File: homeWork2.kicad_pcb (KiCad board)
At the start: 2 copper layers, 125 x 99.9 mm, 43 parts, among them J1 Barrel_Jack_Switch_SMT, U1 LM7805_TO220

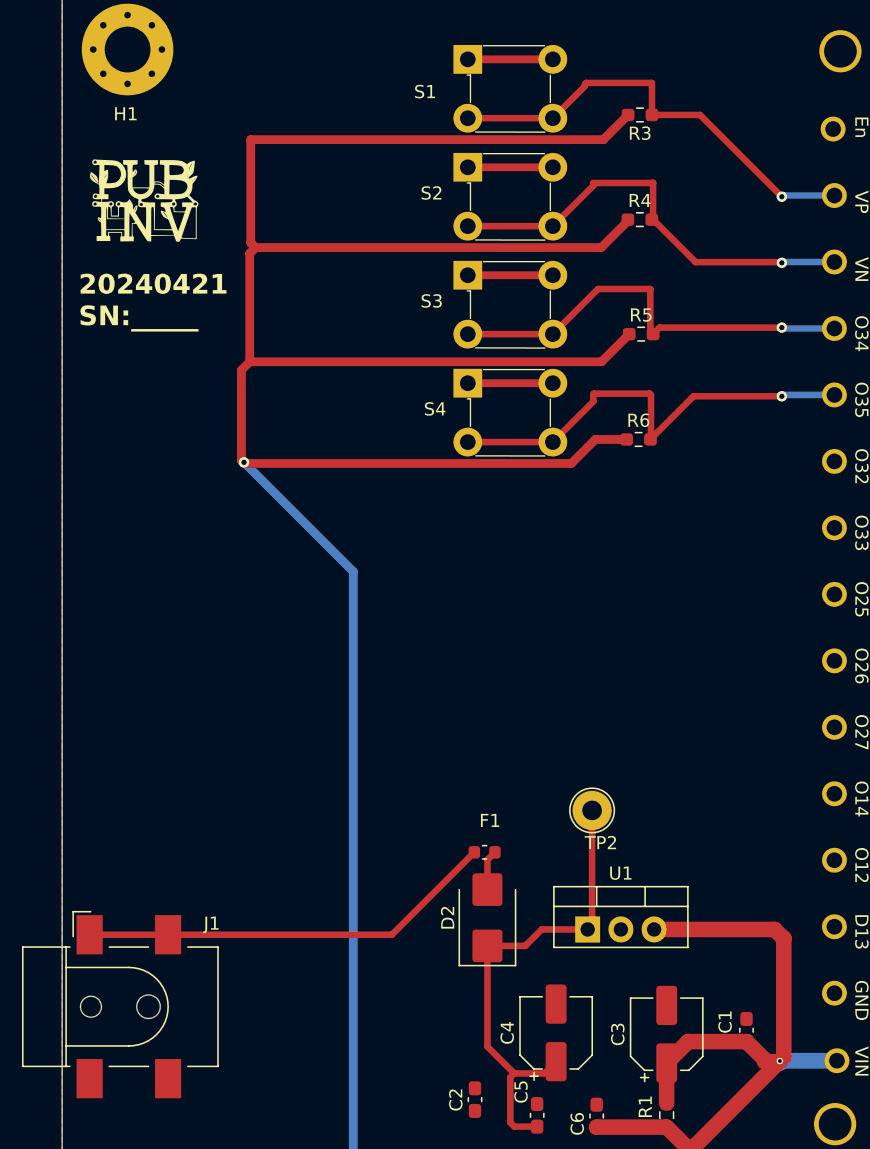
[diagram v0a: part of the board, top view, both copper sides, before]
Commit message: Added text box capturing the calculations for setting the currect in LED.
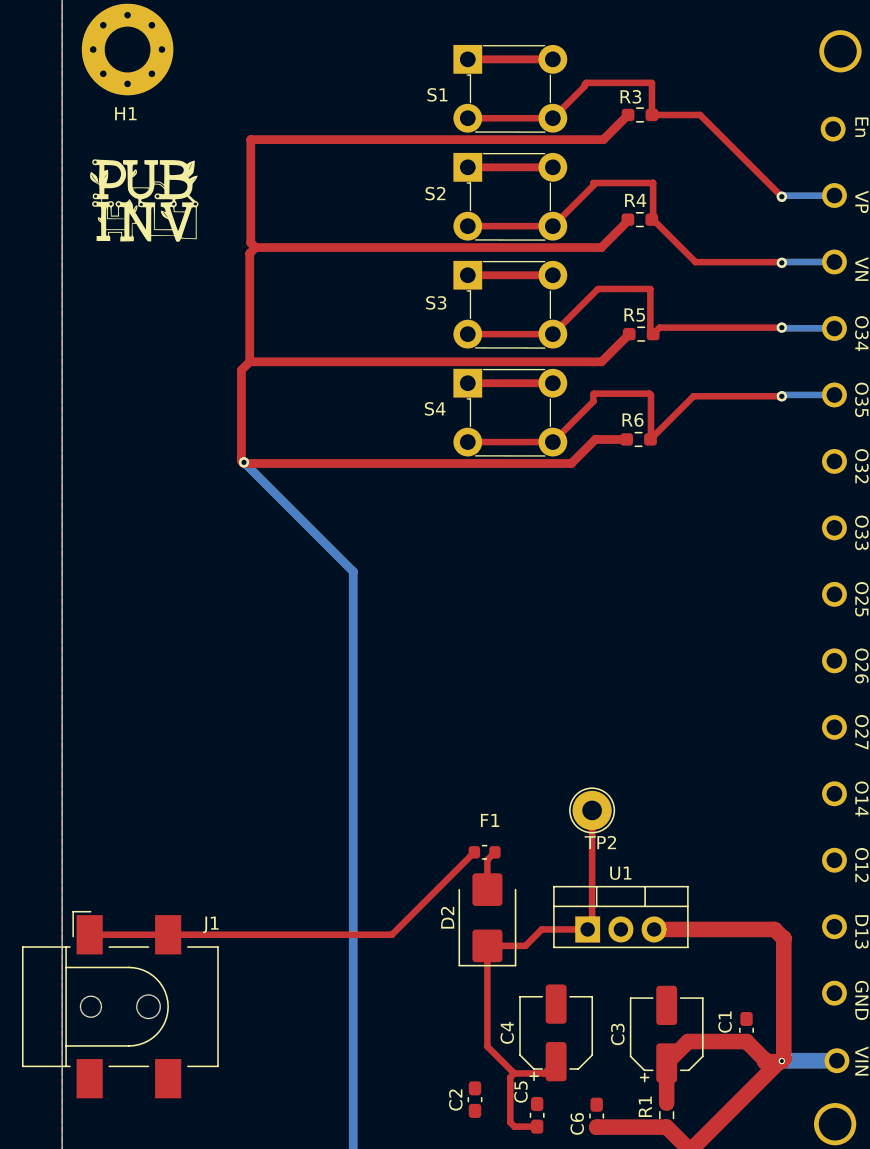
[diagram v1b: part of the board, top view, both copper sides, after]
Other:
- board text removed: "20240421 SN:_____"
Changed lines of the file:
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@@
     (property "ki_keywords" "450-1804-ND FSMJ")
     (attr through_hole)
-    (fp_text reference "S2" (at -2.75 2 180) (layer "F.SilkS")
+    (fp_text reference "S2" (at -2.45 2.05 180) (layer "F.SilkS")
         (effects (font (size 1 1) (thickness 0.15)))
     )
@@
     (property "ki_keywords" "R res resistor")
     (attr smd)
-    (fp_text reference "R4" (at 0 -1.43) (layer "F.SilkS")
+    (fp_text reference "R4" (at -0.35 -1.43) (layer "F.SilkS")
         (effects (font (size 1 1) (thickness 0.15)))
     )
@@
     (property "ki_keywords" "R res resistor")
     (attr smd)
-    (fp_text reference "R3" (at 0 -1.43) (layer "F.SilkS")
+    (fp_text reference "R3" (at 0.7125 1.35) (layer "F.SilkS")
         (effects (font (size 1 1) (thickness 0.15)))
     )
-    (fp_text value "10 k" (at 0 1.43) (layer "F.Fab")
+    (fp_text value "10 k" (at -1.4875 -1.5) (layer "F.Fab")
         (effects (font (size 1 1) (thickness 0.15)))
     )
@@
     (property "ki_keywords" "450-1804-ND FSMJ")
     (attr through_hole)
-    (fp_text reference "S1" (at -3.25 2.5 180) (layer "F.SilkS")
+    (fp_text reference "S1" (at -2.3 2.75 180) (layer "F.SilkS")
         (effects (font (size 1 1) (thickness 0.15)))
     )
@@
     (property "ki_keywords" "R res resistor")
     (attr smd)
-    (fp_text reference "R5" (at 0 -1.43) (layer "F.SilkS")
+    (fp_text reference "R5" (at -0.5 -1.43) (layer "F.SilkS")
         (effects (font (size 1 1) (thickness 0.15)))
     )
@@
     (property "ki_keywords" "450-1804-ND FSMJ")
     (attr through_hole)
-    (fp_text reference "S3" (at -2.75 2 180) (layer "F.SilkS")
+    (fp_text reference "S3" (at -2.4 2.15 180) (layer "F.SilkS")
         (effects (font (size 1 1) (thickness 0.15)))
     )
@@
     (property "ki_keywords" "R res resistor")
     (attr smd)
-    (fp_text reference "R6" (at 0 -1.43) (layer "F.SilkS")
+    (fp_text reference "R6" (at -0.45 -1.45) (layer "F.SilkS")
         (effects (font (size 1 1) (thickness 0.15)))
     )
@@
   (gr_rect (start 50 50) (end 175 149.95)
     (stroke (width 0.1) (type default)) (fill none) (layer "Edge.Cuts"))
-  (gr_text "20240421\nSN:_____" (at 51.25 76.25) (layer "F.SilkS")
-    (effects (font (size 1.5 1.5) (thickness 0.3) bold) (justify left bottom))
-  )
+  (gr_text_box "20240421\nSN:_____"
+    (start 52 72.3) (end 61 79.3) (layer "F.SilkS")
+      (effects (font (size 1 1) (thickness 0.15)) (justify left top))
+    (stroke (width 0.2) (type solid))  )
   (dimension (type aligned) (layer "Dwgs.User")
     (pts (xy 50 150) (xy 170 150))
@@
   (segment (start 86.3 137.3125) (end 84.5625 137.3125) (width 0.5) (layer "F.Cu") (net 2))
   (segment (start 102.3 130.8125) (end 97.8375 130.8125) (width 1.19) (layer "F.Cu") (net 3))
-  (segment (start 104.8 132.35) (end 104.85 132.3) (width 1.19) (layer "F.Cu") (net 3))
   (segment (start 97.75 140.15) (end 97.75 138.9) (width 1.19) (layer "F.Cu") (net 3))
-  (segment (start 105.15 122.95) (end 105.15 132) (width 1.19) (layer "F.Cu") (net 3))
   (segment (start 103.7 132.2125) (end 103.7 132.35) (width 1.19) (layer "F.Cu") (net 3))
+  (segment (start 97.75 139.4) (end 97.75 140.15) (width 1.19) (layer "F.Cu") (net 3))
   (segment (start 91 143.25) (end 92.9125 143.25) (width 1.19) (layer "F.Cu") (net 3))
   (segment (start 96.2 137.35) (end 90.8625 137.35) (width 1.19) (layer "F.Cu") (net 3))
@@
   (segment (start 90.8625 137.35) (end 90.85 137.3625) (width 1.19) (layer "F.Cu") (net 3))
   (segment (start 103.7 132.35) (end 103.8375 132.35) (width 1.19) (layer "F.Cu") (net 3))
-  (segment (start 105.15 132) (end 104.85 132.3) (width 1.19) (layer "F.Cu") (net 3))
   (segment (start 104.445 122.245) (end 105.1 122.9) (width 1.19) (layer "F.Cu") (net 3))
+  (segment (start 105 132.3) (end 104.95 132.35) (width 1.19) (layer "F.Cu") (net 3))
+  (segment (start 104.85 132.3) (end 97.75 139.4) (width 1.19) (layer "F.Cu") (net 3))
   (segment (start 97.8375 130.8125) (end 96.2 132.45) (width 1.19) (layer "F.Cu") (net 3))
+  (segment (start 104.95 132.35) (end 103.7 132.35) (width 1.19) (layer "F.Cu") (net 3))
+  (segment (start 105 132.3) (end 105.15 132.15) (width 1.19) (layer "F.Cu") (net 3))
   (segment (start 97.75 141.75) (end 97.75 140.15) (width 1.19) (layer "F.Cu") (net 3))
   (segment (start 96.2 132.45) (end 96.2 135.525) (width 1.19) (layer "F.Cu") (net 3))
   (segment (start 99.15 143.15) (end 101.85 143.15) (width 1.19) (layer "F.Cu") (net 3))
-  (segment (start 104.85 132.3) (end 97.75 139.4) (width 1.19) (layer "F.Cu") (net 3))
-  (segment (start 97.75 139.4) (end 97.75 140.15) (width 1.19) (layer "F.Cu") (net 3))
-  (segment (start 103.7 132.35) (end 104.8 132.35) (width 1.19) (layer "F.Cu") (net 3))
-  (via (at 104.85 132.3) (size 0.5) (drill 0.3) (layers "F.Cu" "B.Cu") (net 3))
-  (segment (start 104.85 132.3) (end 104.85 132.45) (width 1.19) (layer "B.Cu") (net 3))
-  (segment (start 104.85 132.45) (end 105 132.3) (width 1.19) (layer "B.Cu") (net 3))
+  (segment (start 105 132.3) (end 104.85 132.3) (width 1.19) (layer "F.Cu") (net 3))
+  (segment (start 105.15 132.15) (end 105.15 122.95) (width 1.19) (layer "F.Cu") (net 3))
+  (via (at 105 132.3) (size 0.5) (drill 0.3) (layers "F.Cu" "B.Cu") (net 3))
   (segment (start 105.023 132.277) (end 105 132.3) (width 1.19) (layer "B.Cu") (net 3))
-  (segment (start 105 132.3) (end 104.85 132.3) (width 1.19) (layer "B.Cu") (net 3))
   (segment (start 109.2107 132.277) (end 105.023 132.277) (width 1.19) (layer "B.Cu") (net 3))
   (segment (start 82.5 119.2) (end 82.5 116.925) (width 0.5) (layer "F.Cu") (net 5))

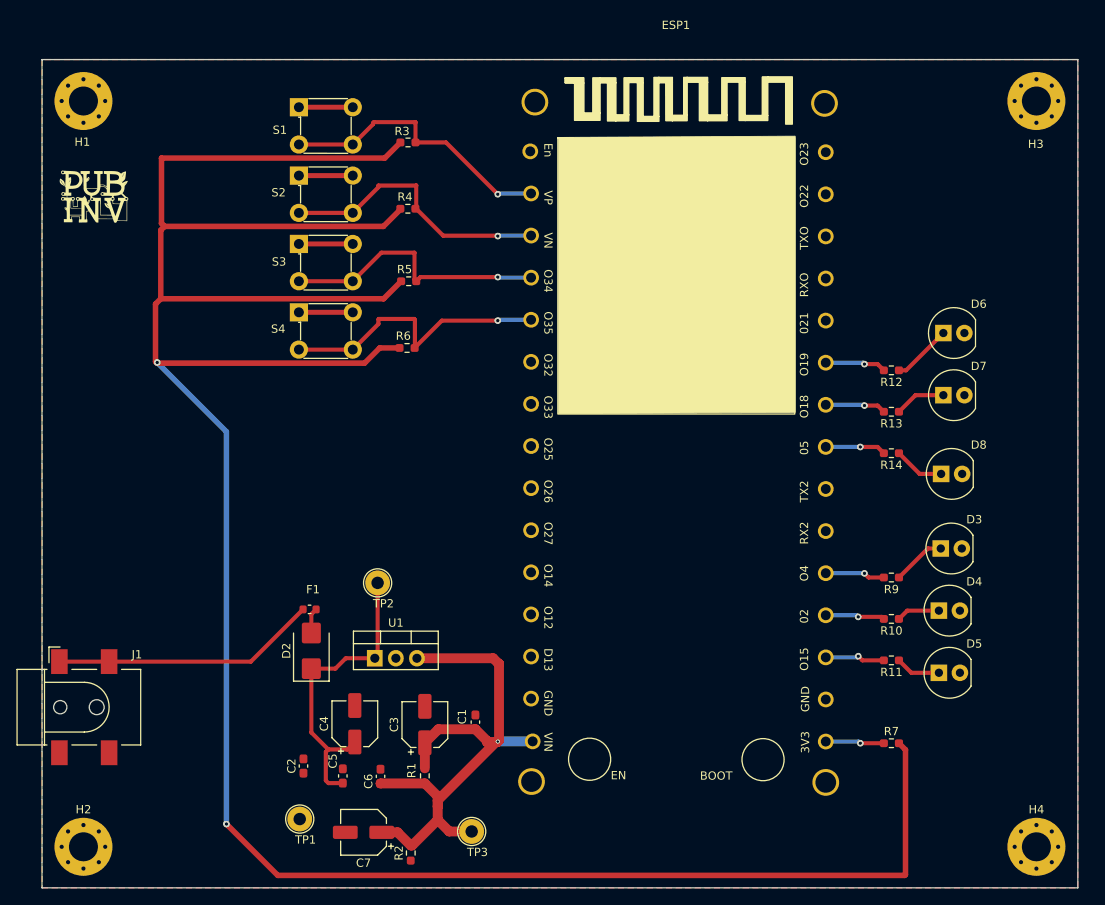
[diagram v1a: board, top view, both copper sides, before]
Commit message: Functions have been added to the switches and LEDs, and silkscreen has been included on the PCB to indicate these functions.
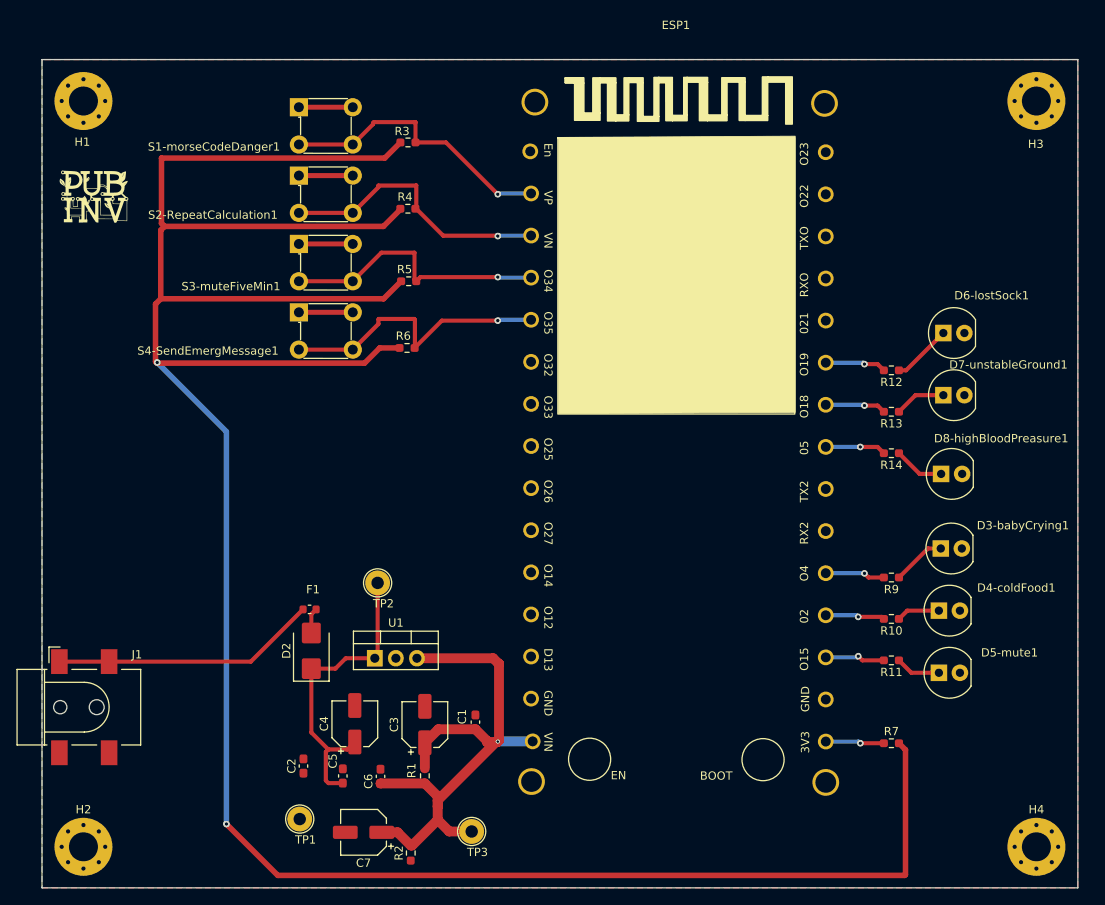
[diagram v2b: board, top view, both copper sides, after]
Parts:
- renumbered D3 to D3-babyCrying1, D4 to D4-coldFood1, D5 to D5-mute1, D6 to D6-lostSock1, D7 to D7-unstableGround1, D8 to D8-highBloodPreasure1, S1 to S1-morseCodeDanger1, S2 to S2-RepeatCalculation1, S3 to S3-muteFiveMin1, S4 to S4-SendEmergMessage1
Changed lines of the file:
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@@
   (net 4 "Net-(D1-Pad1)")
   (net 5 "Net-(D2-A)")
-  (net 6 "Net-(D3-Pad1)")
-  (net 7 "Net-(D4-Pad1)")
-  (net 8 "Net-(D5-Pad1)")
-  (net 9 "Net-(D6-Pad1)")
-  (net 10 "Net-(D7-Pad1)")
-  (net 11 "Net-(D8-Pad1)")
+  (net 6 "Net-(D3-babyCrying1-Pad1)")
+  (net 7 "Net-(D4-coldFood1-Pad1)")
+  (net 8 "Net-(D5-mute1-Pad1)")
+  (net 9 "Net-(D6-lostSock1-Pad1)")
+  (net 10 "Net-(D7-unstableGround1-Pad1)")
+  (net 11 "Net-(D8-highBloodPreasure1-Pad1)")
   (net 12 "unconnected-(ESP1-O13-Pad3)")
   (net 13 "Net-(F1-Pad2)")
@@
       (stroke (width 0.1) (type solid)) (layer "F.Fab"))
     (pad "1" smd roundrect (at -0.9125 0 180) (size 0.975 0.95) (layers "F.Cu" "F.Paste" "F.Mask") (roundrect_rratio 0.25)
-      (net 11 "Net-(D8-Pad1)") (pintype "passive"))
+      (net 11 "Net-(D8-highBloodPreasure1-Pad1)") (pintype "passive"))
     (pad "2" smd roundrect (at 0.9125 0 180) (size 0.975 0.95) (layers "F.Cu" "F.Paste" "F.Mask") (roundrect_rratio 0.25)
       (net 19 "Net-(ESP1-O5)") (pintype "passive"))
@@
     (property "ki_keywords" "160-1772-ND")
     (attr through_hole)
-    (fp_text reference "D6" (at 1.73 -3.5) (layer "F.SilkS")
+    (fp_text reference "D6-lostSock1" (at 3.29 -4.525) (layer "F.SilkS")
         (effects (font (size 1 1) (thickness 0.15)))
     )
@@
       (stroke (width 0.1) (type solid)) (layer "F.Fab"))
     (pad "1" thru_hole rect (at -2.54 0) (size 2 2) (drill 1) (layers "*.Cu" "*.Mask")
-      (net 9 "Net-(D6-Pad1)") (pintype "passive"))
+      (net 9 "Net-(D6-lostSock1-Pad1)") (pintype "passive"))
     (pad "2" thru_hole circle (at 0 0) (size 2 2) (drill 1) (layers "*.Cu" "*.Mask")
       (net 1 "GND") (pintype "passive"))
@@
     (property "ki_keywords" "450-1804-ND FSMJ")
     (attr through_hole)
-    (fp_text reference "S2" (at -2.45 2.05 180) (layer "F.SilkS")
+    (fp_text reference "S2-RepeatCalculation1" (at -10.375 4.75 180) (layer "F.SilkS")
         (effects (font (size 1 1) (thickness 0.15)))
     )
@@
       (stroke (width 0.1) (type solid)) (layer "F.Fab"))
     (pad "1" smd roundrect (at -0.9125 0 180) (size 0.975 0.95) (layers "F.Cu" "F.Paste" "F.Mask") (roundrect_rratio 0.25)
-      (net 9 "Net-(D6-Pad1)") (pintype "passive"))
+      (net 9 "Net-(D6-lostSock1-Pad1)") (pintype "passive"))
     (pad "2" smd roundrect (at 0.9125 0 180) (size 0.975 0.95) (layers "F.Cu" "F.Paste" "F.Mask") (roundrect_rratio 0.25)
       (net 17 "Net-(ESP1-O19)") (pintype "passive"))
@@
       (stroke (width 0.1) (type solid)) (layer "F.Fab"))
     (pad "1" smd roundrect (at -0.9125 0 180) (size 0.975 0.95) (layers "F.Cu" "F.Paste" "F.Mask") (roundrect_rratio 0.25)
-      (net 6 "Net-(D3-Pad1)") (pintype "passive"))
+      (net 6 "Net-(D3-babyCrying1-Pad1)") (pintype "passive"))
     (pad "2" smd roundrect (at 0.9125 0 180) (size 0.975 0.95) (layers "F.Cu" "F.Paste" "F.Mask") (roundrect_rratio 0.25)
       (net 14 "Net-(ESP1-O4)") (pintype "passive"))
@@
       (stroke (width 0.1) (type solid)) (layer "F.Fab"))
     (pad "1" smd roundrect (at -0.9125 0 180) (size 0.975 0.95) (layers "F.Cu" "F.Paste" "F.Mask") (roundrect_rratio 0.25)
-      (net 7 "Net-(D4-Pad1)") (pintype "passive"))
+      (net 7 "Net-(D4-coldFood1-Pad1)") (pintype "passive"))
     (pad "2" smd roundrect (at 0.9125 0 180) (size 0.975 0.95) (layers "F.Cu" "F.Paste" "F.Mask") (roundrect_rratio 0.25)
       (net 15 "Net-(ESP1-O2)") (pintype "passive"))
@@
     (property "ki_keywords" "160-1772-ND")
     (attr through_hole)
-    (fp_text reference "D3" (at 1.5 -3.5) (layer "F.SilkS")
+    (fp_text reference "D3-babyCrying1" (at 7.375 -2.775) (layer "F.SilkS")
         (effects (font (size 1 1) (thickness 0.15)))
     )
@@
       (stroke (width 0.1) (type solid)) (layer "F.Fab"))
     (pad "1" thru_hole rect (at -2.54 0) (size 2 2) (drill 1) (layers "*.Cu" "*.Mask")
-      (net 6 "Net-(D3-Pad1)") (pintype "passive"))
+      (net 6 "Net-(D3-babyCrying1-Pad1)") (pintype "passive"))
     (pad "2" thru_hole circle (at 0 0) (size 2 2) (drill 1) (layers "*.Cu" "*.Mask")
       (net 1 "GND") (pintype "passive"))
@@
     (property "ki_keywords" "450-1804-ND FSMJ")
     (attr through_hole)
-    (fp_text reference "S1" (at -2.3 2.75 180) (layer "F.SilkS")
+    (fp_text reference "S1-morseCodeDanger1" (at -10.25 4.775 180) (layer "F.SilkS")
         (effects (font (size 1 1) (thickness 0.15)))
     )
@@
     (property "ki_keywords" "160-1772-ND")
     (attr through_hole)
-    (fp_text reference "D5" (at 1.73 -3.5) (layer "F.SilkS")
+    (fp_text reference "D5-mute1" (at 5.98 -2.425) (layer "F.SilkS")
         (effects (font (size 1 1) (thickness 0.15)))
     )
@@
       (stroke (width 0.1) (type solid)) (layer "F.Fab"))
     (pad "1" thru_hole rect (at -2.54 0) (size 2 2) (drill 1) (layers "*.Cu" "*.Mask")
-      (net 8 "Net-(D5-Pad1)") (pintype "passive"))
+      (net 8 "Net-(D5-mute1-Pad1)") (pintype "passive"))
     (pad "2" thru_hole circle (at 0 0) (size 2 2) (drill 1) (layers "*.Cu" "*.Mask")
       (net 1 "GND") (pintype "passive"))
@@
     (property "ki_keywords" "450-1804-ND FSMJ")
     (attr through_hole)
-    (fp_text reference "S3" (at -2.4 2.15 180) (layer "F.SilkS")
+    (fp_text reference "S3-muteFiveMin1" (at -8.2 5.125 180) (layer "F.SilkS")
         (effects (font (size 1 1) (thickness 0.15)))
     )
@@
     (property "ki_keywords" "160-1772-ND")
     (attr through_hole)
-    (fp_text reference "D4" (at 1.73 -3.5) (layer "F.SilkS")
+    (fp_text reference "D4-coldFood1" (at 6.805 -2.75) (layer "F.SilkS")
         (effects (font (size 1 1) (thickness 0.15)))
     )
@@
       (stroke (width 0.1) (type solid)) (layer "F.Fab"))
     (pad "1" thru_hole rect (at -2.54 0) (size 2 2) (drill 1) (layers "*.Cu" "*.Mask")
-      (net 7 "Net-(D4-Pad1)") (pintype "passive"))
+      (net 7 "Net-(D4-coldFood1-Pad1)") (pintype "passive"))
     (pad "2" thru_hole circle (at 0 0) (size 2 2) (drill 1) (layers "*.Cu" "*.Mask")
       (net 1 "GND") (pintype "passive"))
@@
     (property "ki_keywords" "160-1772-ND")
     (attr through_hole)
-    (fp_text reference "D7" (at 1.73 -3.5) (layer "F.SilkS")
+    (fp_text reference "D7-unstableGround1" (at 5.315 -3.675) (layer "F.SilkS")
         (effects (font (size 1 1) (thickness 0.15)))
     )
@@
       (stroke (width 0.1) (type solid)) (layer "F.Fab"))
     (pad "1" thru_hole rect (at -2.54 0) (size 2 2) (drill 1) (layers "*.Cu" "*.Mask")
-      (net 10 "Net-(D7-Pad1)") (pintype "passive"))
+      (net 10 "Net-(D7-unstableGround1-Pad1)") (pintype "passive"))
     (pad "2" thru_hole circle (at 0 0) (size 2 2) (drill 1) (layers "*.Cu" "*.Mask")
       (net 1 "GND") (pintype "passive"))
@@
       (stroke (width 0.1) (type solid)) (layer "F.Fab"))
     (pad "1" smd roundrect (at -0.9125 0 180) (size 0.975 0.95) (layers "F.Cu" "F.Paste" "F.Mask") (roundrect_rratio 0.25)
-      (net 8 "Net-(D5-Pad1)") (pintype "passive"))
+      (net 8 "Net-(D5-mute1-Pad1)") (pintype "passive"))
     (pad "2" smd roundrect (at 0.9125 0 180) (size 0.975 0.95) (layers "F.Cu" "F.Paste" "F.Mask") (roundrect_rratio 0.25)
       (net 16 "Net-(ESP1-O15)") (pintype "passive"))
@@
       (stroke (width 0.1) (type solid)) (layer "F.Fab"))
     (pad "1" smd roundrect (at -0.9125 0 180) (size 0.975 0.95) (layers "F.Cu" "F.Paste" "F.Mask") (roundrect_rratio 0.25)
-      (net 10 "Net-(D7-Pad1)") (pintype "passive"))
+      (net 10 "Net-(D7-unstableGround1-Pad1)") (pintype "passive"))
     (pad "2" smd roundrect (at 0.9125 0 180) (size 0.975 0.95) (layers "F.Cu" "F.Paste" "F.Mask") (roundrect_rratio 0.25)
       (net 18 "Net-(ESP1-O18)") (pintype "passive"))
@@
     (property "ki_keywords" "450-1804-ND FSMJ")
     (attr through_hole)
-    (fp_text reference "S4" (at -2.5 2 180) (layer "F.SilkS")
+    (fp_text reference "S4-SendEmergMessage1" (at -10.975 4.65 180) (layer "F.SilkS")
         (effects (font (size 1 1) (thickness 0.15)))
     )
@@
     (property "ki_keywords" "160-1772-ND")
     (attr through_hole)
-    (fp_text reference "D8" (at 2 -3.5) (layer "F.SilkS")
+    (fp_text reference "D8-highBloodPreasure1" (at 4.71 -4.275) (layer "F.SilkS")
         (effects (font (size 1 1) (thickness 0.15)))
     )
@@
       (stroke (width 0.1) (type solid)) (layer "F.Fab"))
     (pad "1" thru_hole rect (at -2.54 0) (size 2 2) (drill 1) (layers "*.Cu" "*.Mask")
-      (net 11 "Net-(D8-Pad1)") (pintype "passive"))
+      (net 11 "Net-(D8-highBloodPreasure1-Pad1)") (pintype "passive"))
     (pad "2" thru_hole circle (at 0 0) (size 2 2) (drill 1) (layers "*.Cu" "*.Mask")
       (net 1 "GND") (pintype "passive"))
